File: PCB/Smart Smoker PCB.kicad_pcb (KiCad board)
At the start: 2 copper layers, 80 x 50 mm, 1 part, among them U1 ESP32-WROOM-32UE_16MB

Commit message: Significant PCB progress
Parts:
- added C1: 22uF 450V 20%, Capacitor_THT:CP_Radial_D16.0mm_P7.50mm, F.Cu at (106.0, 129.8)
- added C2: 1000pF 440VAC Y5P, Capacitor_THT:C_Disc_D9.0mm_W5.0mm_P7.50mm, F.Cu at (132.5, 124.2)
- added C3: 820uF 20% 16V, Capacitor_THT:CP_Radial_D10.0mm_P5.00mm, F.Cu at (104.0, 144.3)
- added C4: 150uF 20% 35V, Capacitor_THT:CP_Radial_D8.0mm_P3.50mm, F.Cu at (145.0, 125.8)
- added C5: 0.1uF 50V X7R 0603, Capacitor_SMD:C_0603_1608Metric, F.Cu at (114.3, 139.8)
- added C6: 0.1uF 50V X7R 0603, Capacitor_SMD:C_0603_1608Metric, F.Cu at (138.8, 116.5)
- added D1: TVS DIODE 7VWM 12VC SMB, Diode_SMD:D_SMB, F.Cu at (145.8, 133.3)
- added D2: LED, LED_SMD:LED_0603_1608Metric, F.Cu at (144.8, 140.0)
- added F1: 300V 1A SlowBlow, Fuse:Fuse_Littelfuse_395Series, F.Cu at (102.8, 119.0)
- added J1: AC_IN, Connector_Molex:Molex_Micro-Fit_3.0_43045-0400_2x02_P3.00mm_Horizontal, F.Cu at (123.1, 130.9)
- added J2: Hopper, Connector_Molex:Molex_Micro-Fit_3.0_43045-0400_2x02_P3.00mm_Horizontal, F.Cu at (141.3, 110.5)
- added J3: Lid, Connector_Molex:Molex_Micro-Fit_3.0_43045-0400_2x02_P3.00mm_Horizontal, F.Cu at (153.6, 110.5)
- added L1: 2.2mH 350mA 3.2Ohm TH, Inductor_THT:L_Radial_D12.0mm_P5.00mm_Fastron_11P, F.Cu at (122.8, 142.5)
- added L2: 2.2uH 7.2A 11.5mOhm, Inductor_SMD:L_Taiyo-Yuden_NR-80xx, F.Cu at (136.8, 132.3)
- added PS1: LS10-13B03R3, Customs Smoker:CONV_LS10-13B03R3, F.Cu at (119.0, 103.5)
- added R1: 6.8Ohm 3W 5% 2512, Resistor_SMD:R_2512_6332Metric, F.Cu at (114.7, 118.7)
- added R2: R_US, Resistor_SMD:R_0603_1608Metric, F.Cu at (144.7, 142.6)
- added TP1: TestPoint_2Pole, TestPoint:TestPoint_2Pads_Pitch5.08mm_Drill1.3mm, F.Cu at (135.3, 145.7)
- added TP2: TestPoint_2Pole, TestPoint:TestPoint_2Pads_Pitch5.08mm_Drill1.3mm, F.Cu at (135.3, 141.0)
- added U2: DG409LEDY-T1-GE3, Customs Smoker:SOIC16_NARROW_VIS, F.Cu at (165.1, 105.7)
- added U3: MAX31855KASA, Package_SO:SOIC-8_3.9x4.9mm_P1.27mm, F.Cu at (165.4, 114.2)
- moved U1 27.0 mm to (168.3, 137.8)

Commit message: PCB layout done
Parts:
- added C10: 1uF 25V X5R 0603, Capacitor_SMD:C_0603_1608Metric, F.Cu at (138.0, 123.8)
- added C11: 0.1uF 50V X7R 0603, Capacitor_SMD:C_0603_1608Metric, F.Cu at (144.2, 106.9)
- added C12: 0.1uF 50V X7R 0603, Capacitor_SMD:C_0603_1608Metric, F.Cu at (133.8, 125.0)
- added C13: 0.1uF 50V X7R 0603, Capacitor_SMD:C_0603_1608Metric, F.Cu at (148.5, 118.8)
- added C14: 0.1uF 50V X7R 0603, Capacitor_SMD:C_0603_1608Metric, F.Cu at (175.8, 124.2)
- added C15: 1uF 25V X5R 0603, Capacitor_SMD:C_0603_1608Metric, F.Cu at (180.5, 101.5)
- added C16: 22uF 450V 20%, Capacitor_THT:CP_Radial_D12.5mm_P5.00mm, F.Cu at (137.5, 139.6)
- added C17: 820uF 20% 16V, Capacitor_THT:CP_Radial_D10.0mm_P5.00mm, F.Cu at (128.6, 106.0)
- added C18: 150uF 20% 35V, Capacitor_THT:CP_Radial_D8.0mm_P3.50mm, F.Cu at (113.7, 105.0)
- added C19: 0.1uF 50V X7R 0603, Capacitor_SMD:C_0603_1608Metric, F.Cu at (112.7, 110.5)
- added C20: 1000pF 440VAC Y5P, Capacitor_THT:C_Disc_D9.0mm_W5.0mm_P7.50mm, F.Cu at (133.2, 114.5)
- added C7: 10uF 16V X5R 0805, Capacitor_SMD:C_0805_2012Metric, F.Cu at (148.5, 111.5)
- added C8: 10uF 16V X5R 0805, Capacitor_SMD:C_0805_2012Metric, F.Cu at (136.7, 114.2)
- added C9: 10uF 16V X5R 0805, Capacitor_SMD:C_0805_2012Metric, F.Cu at (136.7, 112.2)
- added D3: Y 2V 20mA, LED_SMD:LED_0603_1608Metric, F.Cu at (178.5, 111.8)
- added D4: Y/G 2.2V 20mA, LED_SMD:LED_0603_1608Metric, F.Cu at (149.8, 114.0)
- added D5: R 1.8V 2mA 0603, LED_SMD:LED_0603_1608Metric, F.Cu at (152.5, 108.5)
- added H1: MountingHole, MountingHole:MountingHole_3.2mm_M3_DIN965_Pad, F.Cu at (186.0, 104.0)
- added H2: MountingHole, MountingHole:MountingHole_3.2mm_M3_DIN965_Pad, F.Cu at (186.0, 141.0)
- added H3: MountingHole, MountingHole:MountingHole_3.2mm_M3_DIN965_Pad, F.Cu at (104.0, 104.0)
- added H4: MountingHole, MountingHole:MountingHole_3.2mm_M3_DIN965_Pad, F.Cu at (104.0, 141.0)
- added J4: 393570002, Customs Smoker:CONN_393570002_MOL, F.Cu at (180.0, 139.8)
- added J5: 393570002, Customs Smoker:CONN_393570002_MOL, F.Cu at (170.1, 139.8)
- added J6: 393570002, Customs Smoker:CONN_393570002_MOL, F.Cu at (160.3, 139.8)
- added J7: Hopper, Connector_Molex:Molex_Micro-Fit_3.0_43045-0400_2x02_P3.00mm_Horizontal, F.Cu at (180.4, 128.8)
- added J8: Lid, Connector_Molex:Molex_Micro-Fit_3.0_43045-0400_2x02_P3.00mm_Horizontal, F.Cu at (180.4, 117.8)
- added JP1: Jumper_2_Open, Connector_PinHeader_2.54mm:PinHeader_1x02_P2.54mm_Vertical, F.Cu at (148.5, 103.2)
- added Q1: Q_PMOS_GSD, Customs Smoker:VESM_TOS, F.Cu at (140.0, 127.5)
- added Q2: 25V 1.5A Trans, Package_TO_SOT_SMD:SOT-23-3, F.Cu at (158.0, 125.8)
- added Q3: 25V 1.5A Trans, Package_TO_SOT_SMD:SOT-23-3, F.Cu at (154.2, 125.8)
- added Q4: Q_PMOS_GSD, Customs Smoker:VESM_TOS, F.Cu at (135.8, 124.2)
- added Q5: 2N7002T-7-F, Package_TO_SOT_SMD:SOT-23, F.Cu at (141.5, 118.8)
- added Q6: 2N7002T-7-F, Package_TO_SOT_SMD:SOT-23, F.Cu at (145.5, 118.8)
- added R10: 47.5kOhm 1% 0603, Resistor_SMD:R_0603_1608Metric, F.Cu at (143.9, 127.8)
- added R11: 470Ohm 5% 0603, Resistor_SMD:R_0603_1608Metric, F.Cu at (140.6, 129.5)
- added R12: 1kOhm 1% 0603, Resistor_SMD:R_0603_1608Metric, F.Cu at (152.0, 118.8)
- added R13: 10K 1% 0603, Resistor_SMD:R_0603_1608Metric, F.Cu at (150.2, 118.7)
- added R14: 10K 1% 0603, Resistor_SMD:R_0603_1608Metric, F.Cu at (152.3, 105.0)
- added R15: 6.8Ohm 3W 5% 2512, Resistor_SMD:R_2512_6332Metric, F.Cu at (103.0, 132.0)
- added R16: 470Ohm 1% 0603, Resistor_SMD:R_0603_1608Metric, F.Cu at (177.8, 114.5)
- added R17: 140Ohm 1% 0603, Resistor_SMD:R_0603_1608Metric, F.Cu at (150.5, 111.2)
- added R18: 750Ohm 1% 0603, Resistor_SMD:R_0603_1608Metric, F.Cu at (152.4, 106.8)
- added R3: 1kOhm 1% 0603, Resistor_SMD:R_0603_1608Metric, F.Cu at (144.0, 129.5)
- added R4: 10K 1% 0603, Resistor_SMD:R_0603_1608Metric, F.Cu at (158.2, 130.9)
- added R5: 22.1kOhm 1% 0603, Resistor_SMD:R_0603_1608Metric, F.Cu at (144.0, 126.0)
- added R6: 10K 1% 0603, Resistor_SMD:R_0603_1608Metric, F.Cu at (153.0, 130.9)
- added R7: 10K 1% 0603, Resistor_SMD:R_0603_1608Metric, F.Cu at (144.1, 131.2)
- added R8: 0Ohm 0603, Resistor_SMD:R_0603_1608Metric, F.Cu at (156.5, 130.9)
- added R9: 0Ohm 0603, Resistor_SMD:R_0603_1608Metric, F.Cu at (154.8, 130.9)
- added S1: TL1015AF160QG, Customs Smoker:SW_TL1015AF160QG, F.Cu at (173.0, 124.2)
- added S2: TL1015AF160QG, Customs Smoker:SW_TL1015AF160QG, F.Cu at (180.5, 105.5)
- added U4: AMS1117-3.3, Package_TO_SOT_SMD:SOT-223-3_TabPin2, F.Cu at (143.0, 113.2)
- added U5: CP2102N-Axx-xQFN28, Package_DFN_QFN:QFN-28-1EP_5x5mm_P0.5mm_EP3.35x3.35mm, F.Cu at (149.0, 128.5)
- added U6: LTC4412xS6, Package_TO_SOT_SMD:TSOT-23-6, F.Cu at (136.8, 127.0)
- C1: value 22uF 450V 20% -> 0.1uF 50V X7R 0603; footprint Capacitor_THT:CP_Radial_D16.0mm_P7.50mm -> Capacitor_SMD:C_0603_1608Metric
- C2: value 1000pF 440VAC Y5P -> 22uF 10V X5R 0805; footprint Capacitor_THT:C_Disc_D9.0mm_W5.0mm_P7.50mm -> Capacitor_SMD:C_0805_2012Metric
- C3: value 820uF 20% 16V -> 0.1uF 50V X7R 0603; footprint Capacitor_THT:CP_Radial_D10.0mm_P5.00mm -> Capacitor_SMD:C_0603_1608Metric
- C4: value 150uF 20% 35V -> 0.01uF 50V X7R 0603; footprint Capacitor_THT:CP_Radial_D8.0mm_P3.50mm -> Capacitor_SMD:C_0603_1608Metric
- C6: value 0.1uF 50V X7R 0603 -> 4.7uF 25V X5R 0805; footprint Capacitor_SMD:C_0603_1608Metric -> Capacitor_SMD:C_0805_2012Metric
- D1: value TVS DIODE 7VWM 12VC SMB -> SP0503BAHT; footprint Diode_SMD:D_SMB -> Package_TO_SOT_SMD:SOT-143
- D2: value LED -> TVS DIODE 7VWM 12VC SMB; footprint LED_SMD:LED_0603_1608Metric -> Diode_SMD:D_SMB
- F1: value 300V 1A SlowBlow -> 300V 2A SlowBlow
- J1: value AC_IN -> 105017-0001; footprint Connector_Molex:Molex_Micro-Fit_3.0_43045-0400_2x02_P3.00mm_Horizontal -> Customs Smoker:MOLEX_105017-0001
- J2: value Hopper -> 393570002; footprint Connector_Molex:Molex_Micro-Fit_3.0_43045-0400_2x02_P3.00mm_Horizontal -> Customs Smoker:CONN_393570002_MOL
- J3: value Lid -> 393570002; footprint Connector_Molex:Molex_Micro-Fit_3.0_43045-0400_2x02_P3.00mm_Horizontal -> Customs Smoker:CONN_393570002_MOL
- R1: value 6.8Ohm 3W 5% 2512 -> 1kOhm 1% 0603; footprint Resistor_SMD:R_2512_6332Metric -> Resistor_SMD:R_0603_1608Metric
- R2: value R_US -> 1kOhm 1% 0603
- moved C3 64.8 mm to (152.3, 101.0)
- moved R1 64.4 mm to (176.8, 101.5)
- moved TP2 56.1 mm to (183.0, 111.5)
- moved C1 55.7 mm to (161.5, 125.5), turned to 180 degrees
- moved R2 50.7 mm to (176.8, 103.2)
- moved J3 49.8 mm to (113.5, 140.0), turned to 180 degrees
- moved D2 49.6 mm to (104.5, 111.0)
- moved C5 36.1 mm to (146.5, 123.5), turned to -90 degrees
- moved J1 34.3 mm to (141.8, 102.2), turned to 180 degrees
- moved L2 31.5 mm to (121.2, 105.0), turned to 180 degrees
- moved J2 30.7 mm to (150.4, 139.8), turned to 180 degrees
- moved C2 29.0 mm to (152.2, 103.0)
- moved L1 28.4 mm to (105.5, 120.0)
- moved U1 28.2 mm to (165.0, 109.8)
- moved TP1 27.4 mm to (113.6, 129.0), turned to 180 degrees
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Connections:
- C1 pad 1: Net-(PS1-Pad3) -> +3.3V
- C1 pad 2: Net-(PS1-Pad4) -> GND
- C2 pad 1: Net-(PS1-Pad4) -> GND
- C2 pad 2: GND -> +3.3V
- C3 pad 1: Net-(L2-Pad1) -> GND
- C3 pad 2: GND -> +3.3V
- C4 pad 1: +3.3V -> /MUX_OUT_+
- C4 pad 2: GND -> /MUX_OUT_-
- C5 pad 1: +3.3V -> GND
- C5 pad 2: GND -> +3.3V
- C6 pad 1: +3.3V -> GND
- C6 pad 2: GND -> +3.3V
- D1 pad 2: +3.3V -> /USB_DP
- D2 pad 2: Net-(D2-Pad2) -> +3.3VA
- F1 pad 2: Net-(R1-Pad1) -> Net-(F1-Pad2)
- J1 pad 1: /AC_L -> +5V
- J1 pad 2: /AC_N -> /USB_DN
- J1 pad 3: unconnected-(J1-Pad3) -> /USB_DP
- J2 pad 1: /SDA -> /Probe4+
- J2 pad 2: GND -> /Probe4-
- J3 pad 1: /SDA -> /AC_L
- J3 pad 2: GND -> /AC_N
- L2 pad 1: Net-(L2-Pad1) -> Net-(C17-Pad1)
- L2 pad 2: +3.3V -> +3.3VA
- PS1 pad 3: Net-(PS1-Pad3) -> Net-(C16-Pad1)
- PS1 pad 4: Net-(PS1-Pad4) -> Net-(C20-Pad1)
- PS1 pad 6: Net-(L2-Pad1) -> Net-(C17-Pad1)
- R1 pad 1: Net-(R1-Pad1) -> /I2C_SCL
- R1 pad 2: Net-(L1-Pad1) -> +3.3V
- R2 pad 1: +3.3V -> /I2C_SDA
- R2 pad 2: Net-(D2-Pad2) -> +3.3V
- U1 pad 1: unconnected-(U1-Pad1) -> GND
- U1 pad 10: unconnected-(U1-Pad10) -> /IO25
- U1 pad 11: unconnected-(U1-Pad11) -> /IO26
- U1 pad 12: unconnected-(U1-Pad12) -> /IO27
- U1 pad 13: unconnected-(U1-Pad13) -> /IO14
- U1 pad 14: unconnected-(U1-Pad14) -> /IO12
- U1 pad 15: unconnected-(U1-Pad15) -> GND
- U1 pad 16: unconnected-(U1-Pad16) -> /IO13
- U1 pad 2: unconnected-(U1-Pad2) -> +3.3V
- U1 pad 23: unconnected-(U1-Pad23) -> /IO15
- U1 pad 24: unconnected-(U1-Pad24) -> /IO2
- U1 pad 25: unconnected-(U1-Pad25) -> /IO0
- U1 pad 26: unconnected-(U1-Pad26) -> /IO4
- U1 pad 27: unconnected-(U1-Pad27) -> /IO16
- U1 pad 28: unconnected-(U1-Pad28) -> /IO17
- U1 pad 29: unconnected-(U1-Pad29) -> /SPI_CS
- U1 pad 3: unconnected-(U1-Pad3) -> /EN
- U1 pad 30: unconnected-(U1-Pad30) -> /SPI_SCK
- U1 pad 31: unconnected-(U1-Pad31) -> /SPI_MISO
- U1 pad 33: unconnected-(U1-Pad33) -> /I2C_SDA
- U1 pad 34: unconnected-(U1-Pad34) -> /RXD0
- U1 pad 35: unconnected-(U1-Pad35) -> /TXD0
- U1 pad 36: unconnected-(U1-Pad36) -> /I2C_SCL
- U1 pad 37: unconnected-(U1-Pad37) -> /IO23
- U1 pad 38: unconnected-(U1-Pad38) -> GND
- U1 pad 39: unconnected-(U1-Pad39) -> GND
- U1 pad 4: unconnected-(U1-Pad4) -> /I36
- U1 pad 40: unconnected-(U1-Pad40) -> GND
- U1 pad 41: unconnected-(U1-Pad41) -> GND
- U1 pad 42: unconnected-(U1-Pad42) -> GND
- U1 pad 43: unconnected-(U1-Pad43) -> GND
- U1 pad 44: unconnected-(U1-Pad44) -> GND
- U1 pad 45: unconnected-(U1-Pad45) -> GND
- U1 pad 46: unconnected-(U1-Pad46) -> GND
- U1 pad 47: unconnected-(U1-Pad47) -> GND
- U1 pad 5: unconnected-(U1-Pad5) -> /I39
- U1 pad 6: unconnected-(U1-Pad6) -> /I34
- U1 pad 7: unconnected-(U1-Pad7) -> /I35
- U1 pad 8: unconnected-(U1-Pad8) -> /IO32
- U1 pad 9: unconnected-(U1-Pad9) -> /IO33
- U2 pad 1: unconnected-(U2-Pad1) -> /IO2
- U2 pad 10: unconnected-(U2-Pad10) -> /Probe4+
- U2 pad 11: unconnected-(U2-Pad11) -> /Probe3+
- U2 pad 12: unconnected-(U2-Pad12) -> /Probe2+
- U2 pad 13: unconnected-(U2-Pad13) -> /Probe1+
- U2 pad 14: unconnected-(U2-Pad14) -> +3.3V
- U2 pad 15: unconnected-(U2-Pad15) -> GND
- U2 pad 16: unconnected-(U2-Pad16) -> /IO15
- U2 pad 2: unconnected-(U2-Pad2) -> +3.3V
- U2 pad 3: unconnected-(U2-Pad3) -> GND
- U2 pad 4: unconnected-(U2-Pad4) -> /Probe1-
- U2 pad 5: unconnected-(U2-Pad5) -> /Probe2-
- U2 pad 6: unconnected-(U2-Pad6) -> /Probe3-
- U2 pad 7: unconnected-(U2-Pad7) -> /Probe4-
- U2 pad 8: unconnected-(U2-Pad8) -> /MUX_OUT_-
- U2 pad 9: unconnected-(U2-Pad9) -> /MUX_OUT_+
- U3 pad 2: unconnected-(U3-Pad2) -> /MUX_OUT_-
- U3 pad 3: unconnected-(U3-Pad3) -> /MUX_OUT_+
- U3 pad 5: unconnected-(U3-Pad5) -> /SPI_SCK
- U3 pad 6: unconnected-(U3-Pad6) -> /SPI_CS
- U3 pad 7: unconnected-(U3-Pad7) -> /SPI_MISO
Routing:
- added copper zone on In2.Cu, net +3.3V
- added copper zone on B.Cu, net GND
- added copper zone on F.Cu, net GND
- added copper zone on In1.Cu, net GND
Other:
- board size 80 x 50 mm -> 90 x 45 mm
- copper layers 2 -> 4

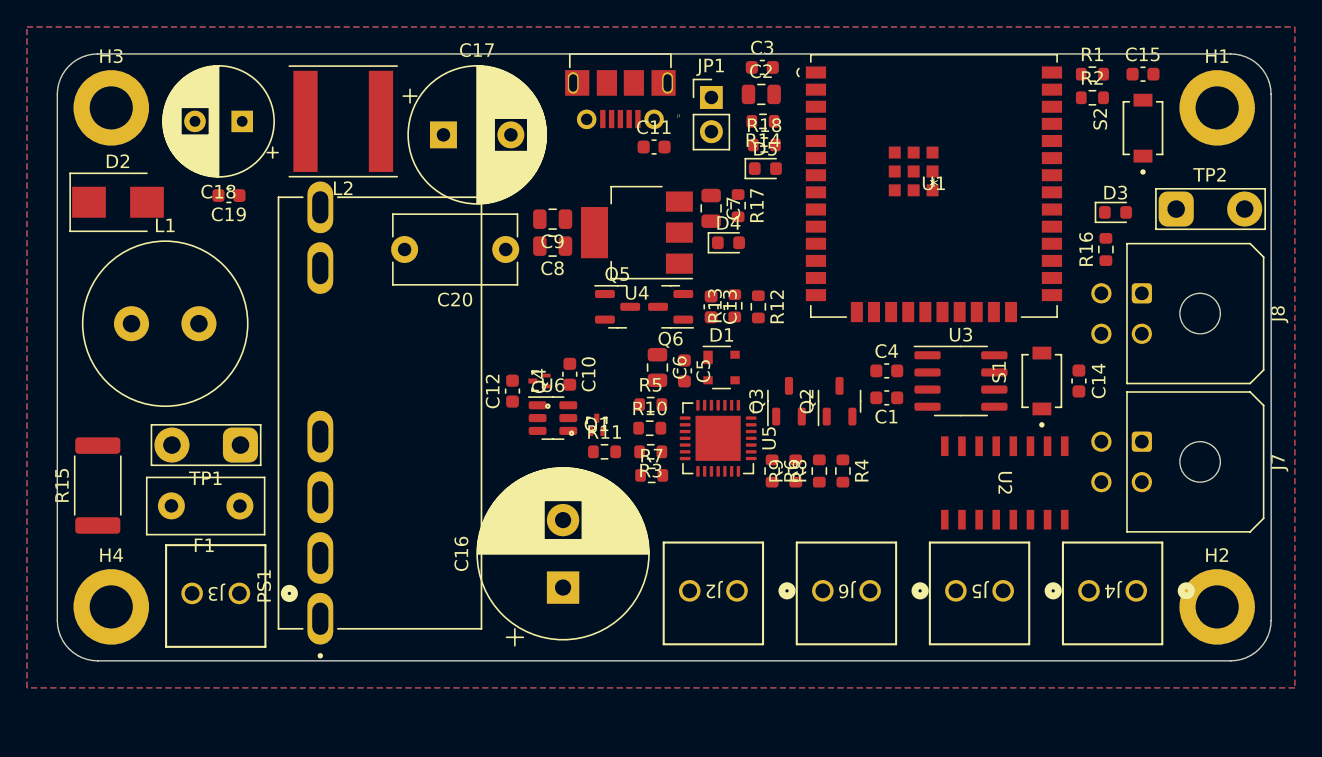
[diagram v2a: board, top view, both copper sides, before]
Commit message: 46 traces left for routing main pcb
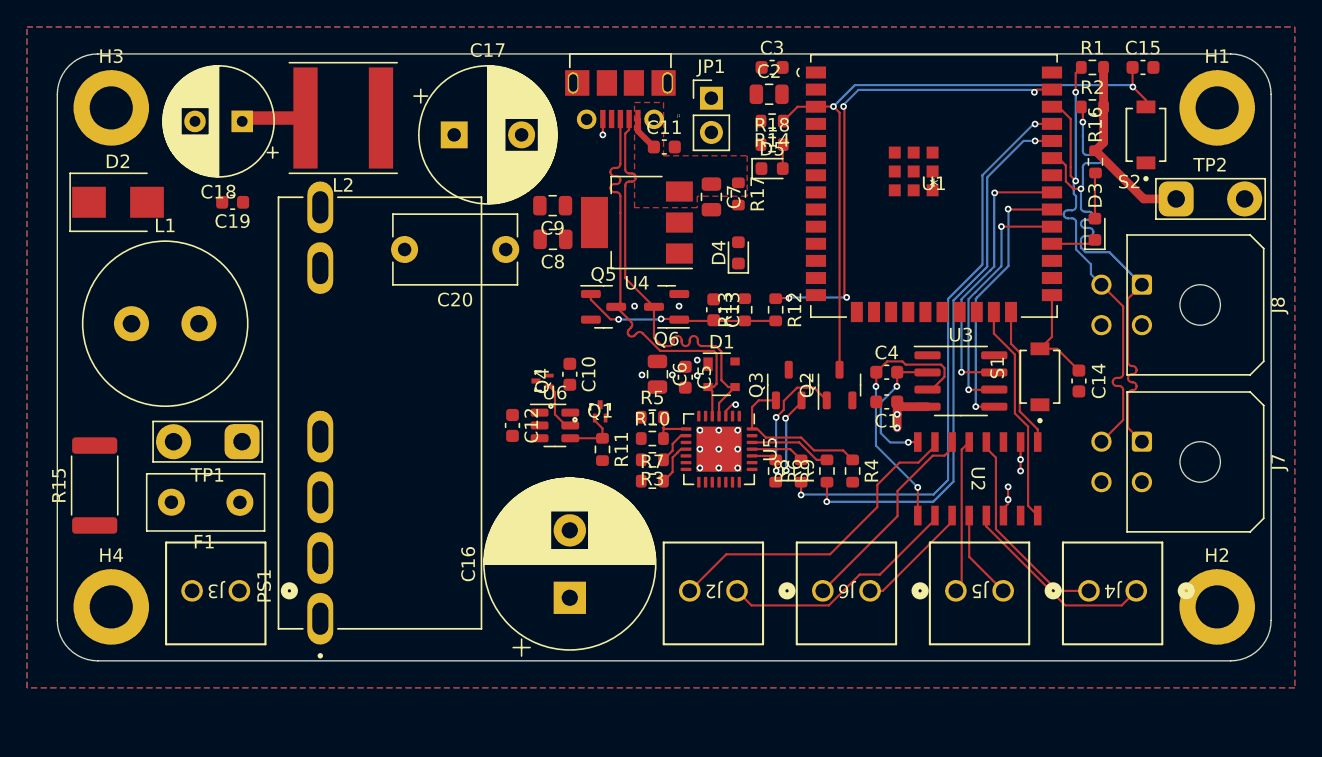
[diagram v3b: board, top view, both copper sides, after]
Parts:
- moved R16 6.55 mm to (177.0, 108.0), turned to -90 degrees
- moved C12 2.55 mm to (133.8, 127.5), turned to -90 degrees
- moved R9 2.32 mm to (157.1, 130.9)
- moved U2 2.02 mm to (168.2, 131.5)
- moved D3 1.97 mm to (176.9, 113.0), turned to 90 degrees
- moved R8 1.35 mm to (155.2, 130.9)
- moved R12 1.30 mm to (153.3, 119.0)
- moved Q3 1.20 mm to (154.2, 124.5)
- moved Q2 1.20 mm to (158.0, 124.5)
- moved D4 1.05 mm to (150.5, 114.8), turned to 90 degrees
- moved Q5 1.04 mm to (140.5, 118.8)
- moved Q1 1.03 mm to (140.2, 126.5)
- moved C9 1.00 mm to (136.7, 111.2)
- moved R5 0.94 mm to (144.1, 126.9)
- moved C16 0.91 mm to (138.0, 140.3)
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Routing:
- net /EN: track 0.00 -> 50.1 mm, vias 0 -> 2
- net /TXD0: track 0.00 -> 42.7 mm, vias 0 -> 2
- net /RXD0: track 0.00 -> 41.0 mm, vias 0 -> 2
- net /I2C_SCL: track 0.00 -> 38.9 mm, vias 0 -> 2
- net /I2C_SDA: track 0.00 -> 38.8 mm, vias 0 -> 2
- net /IO23: track 0.00 -> 35.7 mm, vias 0 -> 4
- net /USB_DN: track 0.00 -> 31.5 mm
- net /USB_DP: track 0.00 -> 31.1 mm
- net /Probe4-: track 0.00 -> 23.9 mm
- net +3.3V: track 0.00 -> 22.7 mm, vias 0 -> 6
- net /SPI_MISO: track 0.00 -> 21.1 mm, vias 0 -> 2
- net /SPI_SCK: track 0.00 -> 20.3 mm, vias 0 -> 2
- net /MUX_OUT_+: track 0.00 -> 19.8 mm, vias 0 -> 2
- net /SPI_CS: track 0.00 -> 18.8 mm, vias 0 -> 2
- net /Probe4+: track 0.00 -> 18.1 mm
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- added copper zone on F.Cu, net +5V

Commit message: Main PCB ready for review
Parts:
- moved C19 6.93 mm to (106.8, 108.0)
- moved C10 0.50 mm to (138.5, 123.8)
- moved C2 0.25 mm to (152.5, 103.0)
- moved C3 0.25 mm to (152.8, 101.0)
- moved D2 0.25 mm to (104.5, 111.2)
- moved D5 0.25 mm to (152.8, 108.5)
- moved R14 0.25 mm to (152.8, 105.0)
- moved R18 0.25 mm to (152.8, 106.7)
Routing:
- net /IO4: track 4.13 -> 60.7 mm, vias 0 -> 2
- net +5V: track 2.57 -> 43.2 mm, vias 0 -> 10
- net Net-(C20-Pad1): track 0.00 -> 36.2 mm
- net +3.3VA: track 4.80 -> 32.9 mm, vias 0 -> 11
- net +3.3VP: track 0.00 -> 23.6 mm, vias 0 -> 4
- net /AC_N: track 0.00 -> 22.7 mm
- net /IO0: track 7.90 -> 29.9 mm, vias 0 -> 2
- net Net-(C16-Pad1): track 0.00 -> 21.6 mm
- net Net-(L1-Pad2): track 0.00 -> 21.1 mm
- net Net-(C13-Pad2): track 14.8 -> 34.9 mm
- net +3.3V: track 22.7 -> 33.5 mm, vias 6 -> 26
- net Net-(L1-Pad1): track 0.00 -> 10.2 mm
- net GND: track 2.49 -> 11.6 mm, vias 17 -> 69
- net Net-(Q2-Pad2): track 0.00 -> 6.70 mm
- net Net-(F1-Pad2): track 0.00 -> 6.40 mm
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- added copper zone on B.Cu, net +3.3V
- added copper zone on F.Cu, net +3.3V
- added copper zone on B.Cu, net +3.3VA
- added copper zone on F.Cu, net +3.3VA
- added copper zone on B.Cu, net +3.3VP
- added copper zone on F.Cu, net +3.3VP
- added copper zone on B.Cu, net +5V
- added copper zone on B.Cu, net /AC_L
- added copper zone on F.Cu, net /AC_L
- added copper zone on B.Cu, net Net-(C17-Pad1)
- added copper zone on F.Cu, net Net-(C17-Pad1)

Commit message: Main pcb reviewed
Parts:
- added J2: 393570002, Customs Smoker:CONN_393570002_MOL, F.Cu at (145.0, 139.8)
- added JP2: Jumper_3_Open, Jumper:SolderJumper-3_P1.3mm_Open_RoundedPad1.0x1.5mm, F.Cu at (146.8, 133.7)
- moved J4 4.50 mm to (109.0, 139.8), turned to 0 degrees
- moved J5 2.75 mm to (177.2, 139.8), turned to 0 degrees
- moved J3 2.66 mm to (153.1, 139.8), turned to 0 degrees
- moved C16 2.00 mm to (136.0, 140.3)
- moved PS1 1.42 mm to (118.1, 126.6)
- moved D5 1.14 mm to (151.7, 108.0)
- moved R18 1.10 mm to (151.7, 106.3)
- moved R14 1.06 mm to (151.7, 104.7)
- moved C2 1.04 mm to (151.5, 102.9)
- moved C3 1.03 mm to (151.7, 101.0)
- moved J6 0.95 mm to (169.2, 139.8), turned to 0 degrees
- moved J7 0.86 mm to (161.1, 139.8), turned to 0 degrees
- moved C11 0.73 mm to (144.3, 106.9)
- moved H1 0.71 mm to (186.5, 103.5)
- moved H2 0.71 mm to (186.5, 141.5)
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- renumbered J2 to J3, J3 to J4, J4 to J5, J5 to J6, J6 to J7, J7 to J8, J8 to J9
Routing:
- net /AC_L: track 0.00 -> 13.0 mm, vias 2 -> 0
- net /Probe4-: track 23.6 -> 15.6 mm
- net /AC_G: track 0.00 -> 6.35 mm
- net /TRG_GND: track 0.00 -> 6.35 mm
- net GND: track 11.6 -> 17.6 mm, vias 69 -> 76
- net /Probe1-: track 15.1 -> 19.9 mm
- net /AC_N: track 22.7 -> 19.1 mm
- net /Probe1+: track 14.8 -> 11.4 mm
- net /Probe3-: track 15.1 -> 12.3 mm
- net /Probe2-: track 10.8 -> 13.1 mm
- net +3.3V: track 33.5 -> 35.6 mm, vias 26 -> 28
- net /EN: track 50.4 -> 51.3 mm
- net /Probe3+: track 8.21 -> 8.96 mm
- net Net-(L1-Pad2): track 21.1 -> 20.4 mm
- net Net-(C16-Pad2): track 36.2 -> 36.8 mm
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- removed copper zone on B.Cu, net /AC_L
- removed copper zone on F.Cu, net /AC_L
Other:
- board text added: "+3.3V"
- board text added: "+5V"
- board text added: "0V"
- board text added: "90 x 45mm H M3x83x38mm"
- board text added: "AC +"
- board text added: "AC N"
- board text added: "AC-"
- board text added: "BOOT"
- board text added: "ESP32-WROOM-32UE"
- board text added: "GPIO17"
- board text added: "HOPPER"
- board text added: "LID"
- board text added: "P1+"
- board text added: "P1-"
- board text added: "P2+"
- board text added: "P2-"
- board text added: "P3+"
- board text added: "P3-"
- board text added: "P4+"
- board text added: "P4-"
- board text added: "RESET"
- board text added: "SMART SMOKER REV A MAY 2023"
- board text added: "Smart Smoker PCB REV A May 2023"
- board text added: "TRG-"
- board text added: "USR"

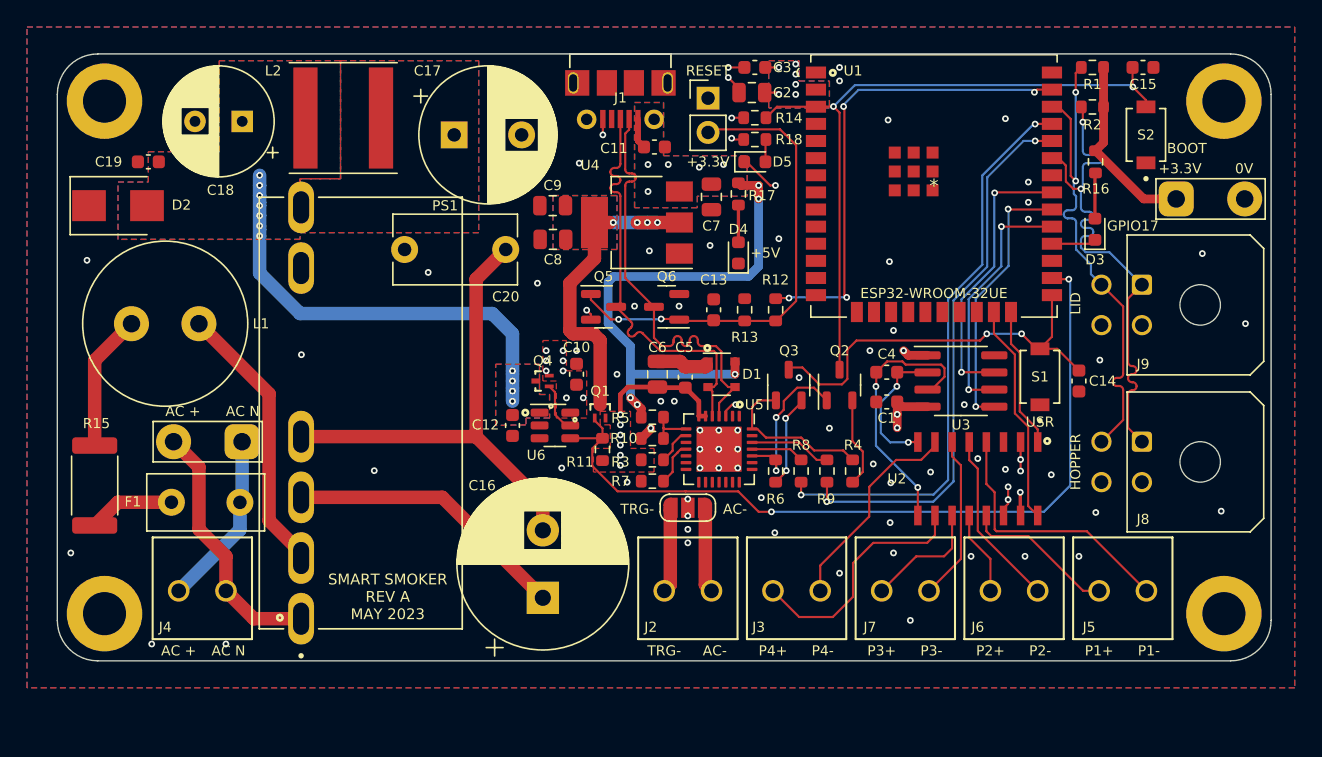
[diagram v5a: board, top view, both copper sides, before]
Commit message: 3x PCB ready for gerberization
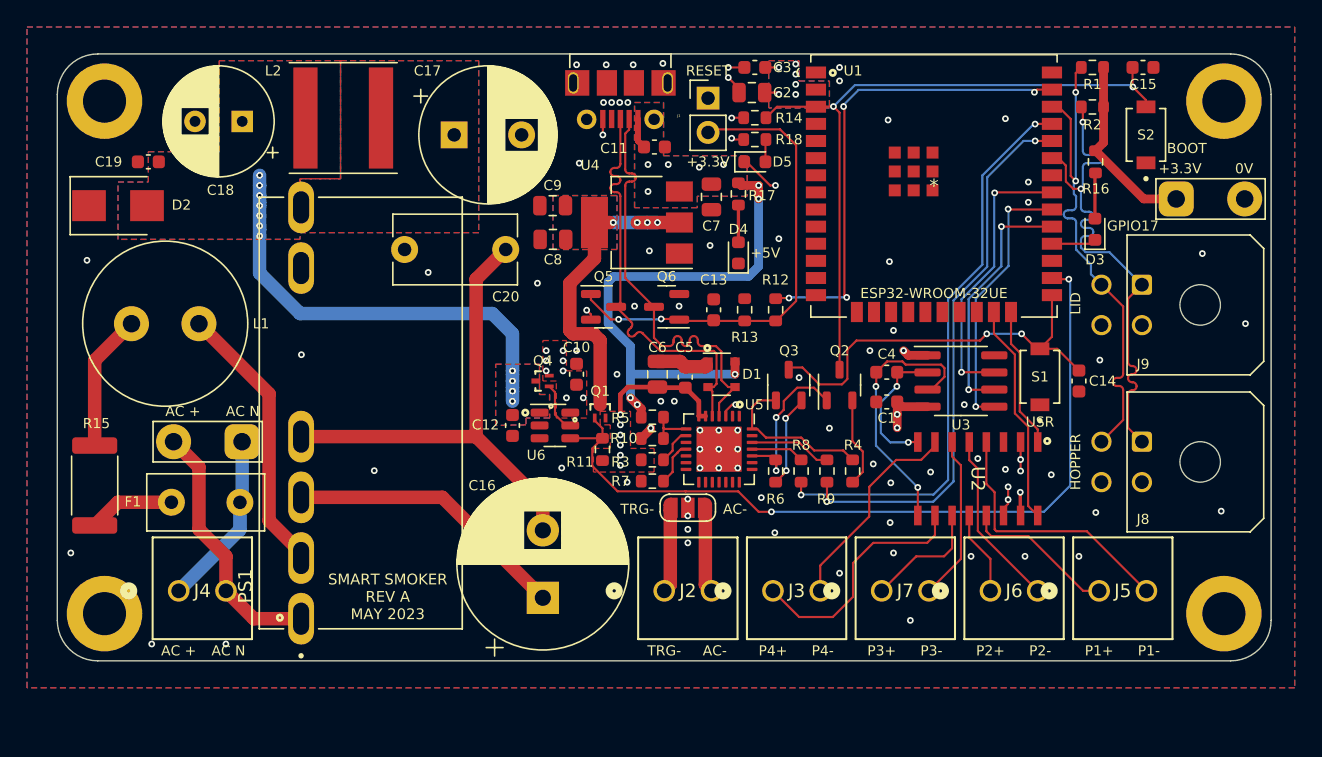
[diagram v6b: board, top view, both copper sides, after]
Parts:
- R1, R2: value 1kOhm 1% 0603 -> 1.8kOhm 1% 0603
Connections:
- J1 pad P$1: (no net) -> GND
- J1 pad P$10: (no net) -> GND
- J1 pad P$11: (no net) -> GND
- J1 pad P$12: (no net) -> GND
- J1 pad P$13: (no net) -> GND
- J1 pad P$2: (no net) -> GND
- J1 pad P$8: (no net) -> GND
- J1 pad P$9: (no net) -> GND
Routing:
- net GND: vias 76 -> 84
